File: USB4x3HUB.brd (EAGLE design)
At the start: 70 x 70 mm, 93 parts, among them IC1 IC_USB_TUSB2036, IC10 IC_TTL_SINGLE_74_139_FLAT, IC2 IC_USB_FSUSB74, IC3 IC_POWER_TPS2041C, IC4 IC_POWER_TPS2041C, IC5 IC_POWER_TPS2041C, IC6 LDO4_3.3_SOT223, IC7 LDO4_5.0_SOT223, IC8 LDO4_5.0_SOT223, IC9 LDO4_5.0_SOT223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

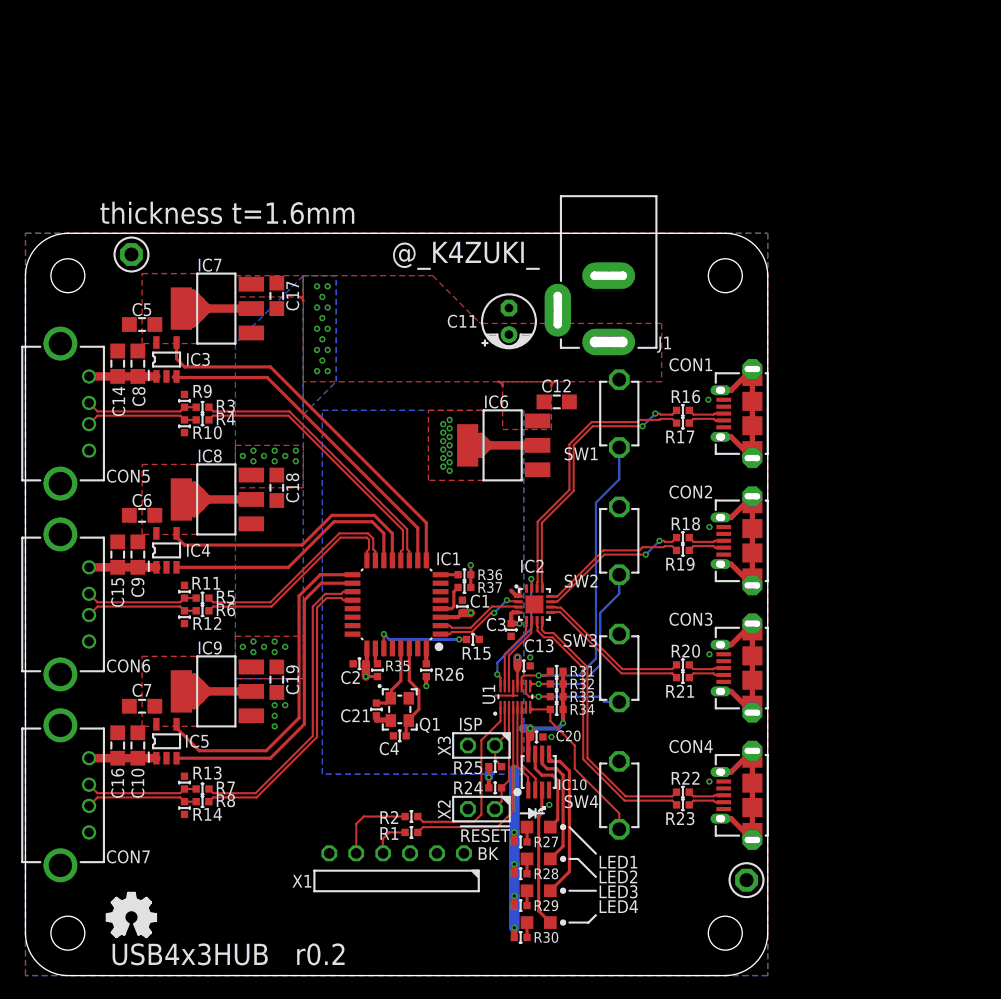
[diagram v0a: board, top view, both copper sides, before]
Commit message: [ r0.3 ] move IC1 and surroundings; replace U1 to use TSSOP(JDH16); ICON_REVISION
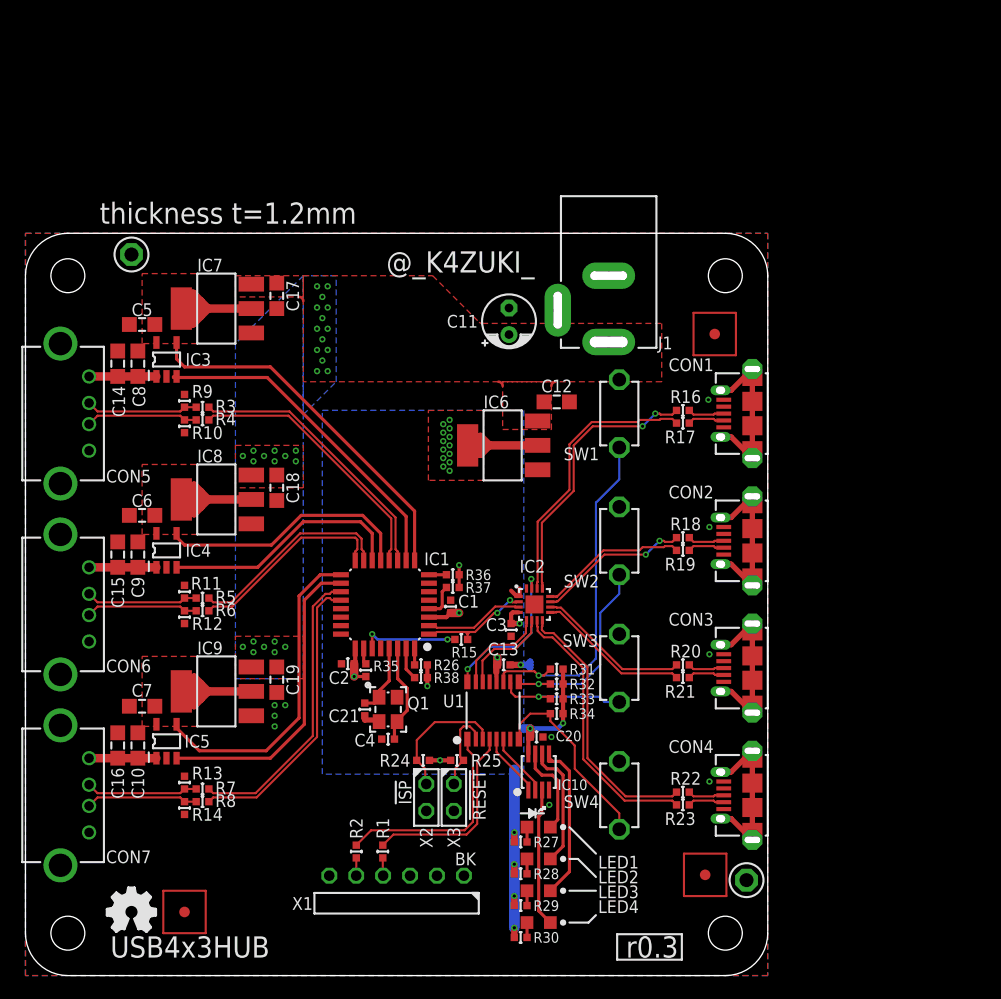
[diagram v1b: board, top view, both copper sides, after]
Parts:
- removed U$1: ICON_OSHW, mylib:ICON_OSHW
- added ICON1: OSHW, mylib:ICON_OSHW
- added ICON2: r0.3, mylib:ICON_REVISION
- added R38: (no value), mylib:C0402
- added TP100, TP101, TP102: (no value), mylib:FIDUCIAL
- IC1: value IC_USB_TUSB2036 -> (none)
- IC2: value IC_USB_FSUSB74 -> (none)
- IC3, IC4, IC5: value IC_POWER_TPS2041C -> (none)
- IC6: value LDO4_3.3_SOT223 -> 3.3V
- IC7, IC8, IC9: value LDO4_5.0_SOT223 -> 5V
- LED1: value (none) -> RD
- LED2: value (none) -> BL
- LED3: value (none) -> GR
- LED4: value (none) -> YL
- Q1: value (none) -> 48M/3225; device mylib:CLOCK_2520 -> mylib:CLOCK_3225
- SW1: value TACTSW2_RD_P807X -> RD
- SW2: value TACTSW2_BL_P807X -> BL
- SW3: value TACTSW2_GR_P807X -> GR
- SW4: value TACTSW2_YL_P807X -> YL
- U1: value IC_LPC81X_16 -> LPC812M101JDH16; device mylib:XSON16_0.4P3.2X2.5 -> mylib:SOT65P510X450X110-16N
- moved R24 7.28 mm to (37.5, 20.3), turned to 0 degrees
- moved R2 6.16 mm to (31.2, 11.7), turned to 90 degrees
- moved X3 5.55 mm to (40.4, 16.8), turned to 90 degrees
- moved X2 5.32 mm to (37.8, 16.8), turned to 90 degrees
- moved R25 3.65 mm to (40.7, 20.3)
- moved R1 3.24 mm to (33.7, 11.7), turned to 90 degrees
- moved U1 2.47 mm to (44.1, 25.0), turned to 0 degrees
- moved X1 2.10 mm to (35.0, 7.90)
- moved C13 1.90 mm to (45.1, 29.3)
- moved C4 1.14 mm to (34.2, 22.3)
- moved C1 1.10 mm to (40.1, 34.8)
- moved C2 1.10 mm to (30.4, 29.4)
- moved C21 1.10 mm to (32.0, 25.1)
- moved IC1 1.10 mm to (33.9, 35.0)
- moved R15 1.10 mm to (41.1, 31.7)
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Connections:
- new net N$63: IC1.31, R38.2
- net 3.3V: now also R38.1
- net GND: no longer IC1.31
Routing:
- net <-RX: track 7.67 -> 1.68 mm
- net N$63: track 0.00 -> 3.08 mm
- net TGT_TX: track 17.3 -> 19.9 mm
- net !RESET!: track 10.2 -> 12.7 mm
- net LSEL2: track 8.35 -> 6.04 mm
- net !OE!: track 12.5 -> 14.7 mm
- net LSEL1: track 8.22 -> 6.04 mm
- net ->TX: track 3.79 -> 1.69 mm
- net SEL1: track 7.05 -> 9.01 mm
- net SW1: track 30.6 -> 32.6 mm
- net ISP: track 6.24 -> 8.19 mm
- net SW3: track 10.9 -> 12.8 mm
- net SEL0: track 7.09 -> 8.91 mm
- net SW4: track 16.7 -> 18.4 mm
- net TGT_RX: track 19.6 -> 18.2 mm
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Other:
- board text added: "!ISP!"
- board text added: "thickness t=1.2mm"
- board text removed: "ISP"
- board text removed: "r0.2"
- board text removed: "thickness t=1.6mm"

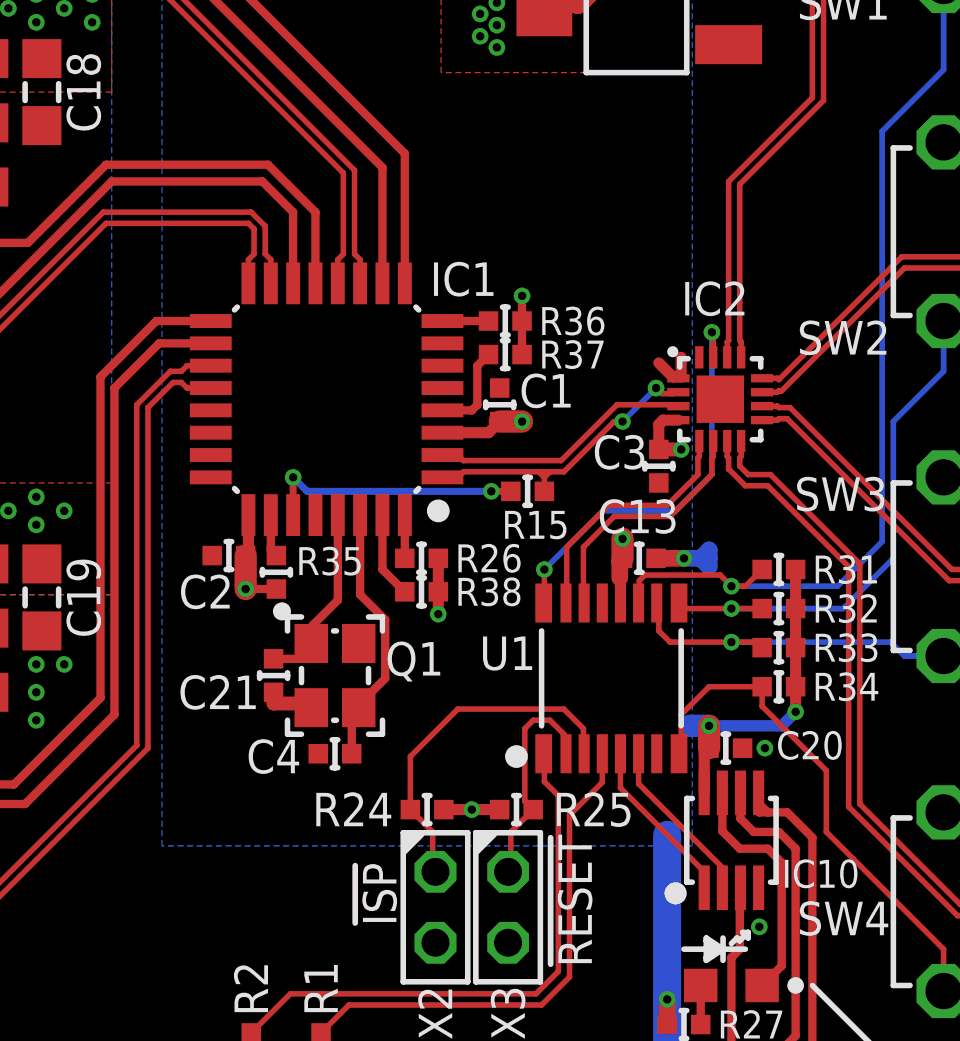
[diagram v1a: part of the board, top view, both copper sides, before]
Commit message: [ r0.3 ] update BOM; fix HUB BUS line
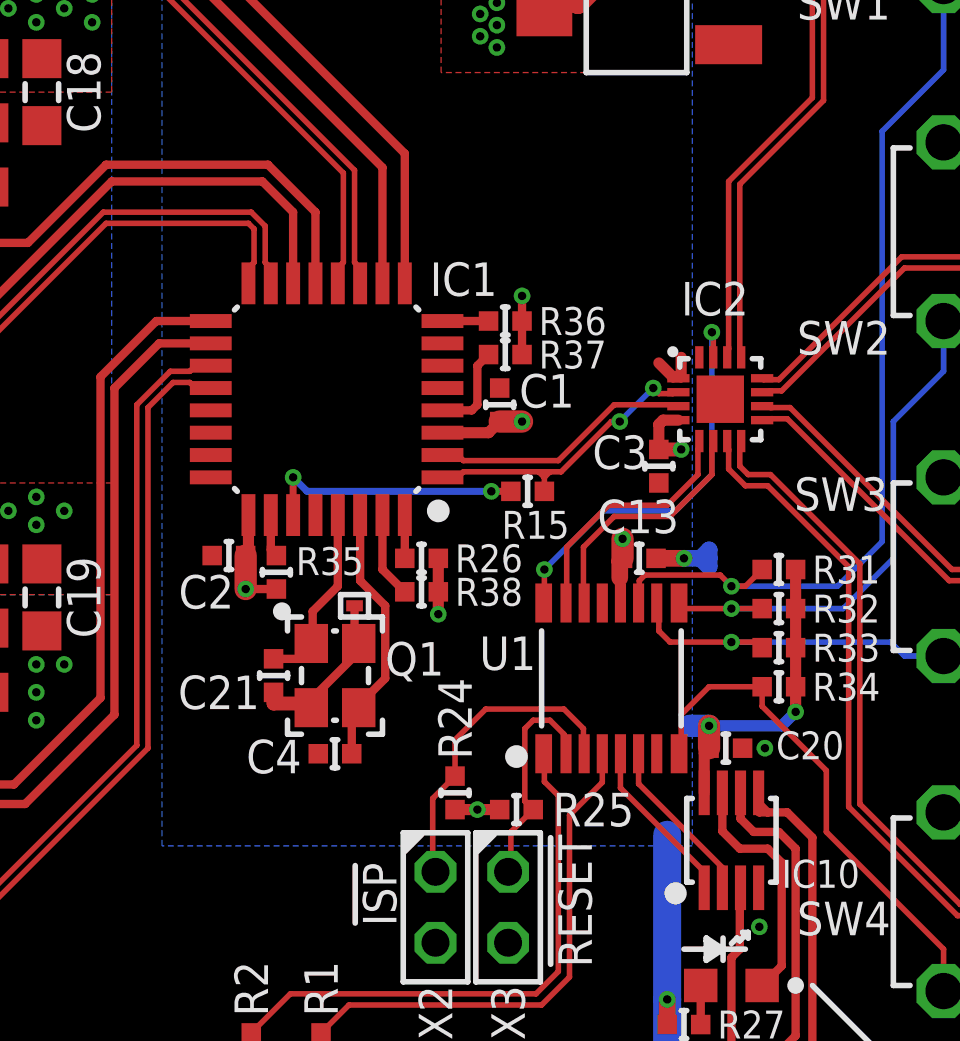
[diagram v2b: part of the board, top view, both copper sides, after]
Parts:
- added TP3: (no value), mylib:TP06RECT
- added U$1: e64d5c4, git-revision:GIT-REVISION
- R15: value (none) -> 1.5k/1005
- moved R24 1.17 mm to (38.5, 20.9), turned to 270 degrees
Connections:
- net GND: now also TP3.TP
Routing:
- net GND: track 6.91 -> 11.3 mm
- net !RESET!: track 12.7 -> 11.4 mm

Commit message: [ r0.3 ] library update
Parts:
- GIT1: value e64d5c4 -> 9ed6508
- IC10: value IC_TTL_SINGLE_74_139_FLAT -> SN74LVC1G139DCUR
- ICON2: device mylib:ICON_REVISION -> mylib:ICON_REVISION2.0
- TP1, TP2: value TPPAD1-13 -> (none); device testpad_local:P1-13 -> mylib:TP_4020
- turned TP1 to 90 degrees
- renumbered U$1 to GIT1

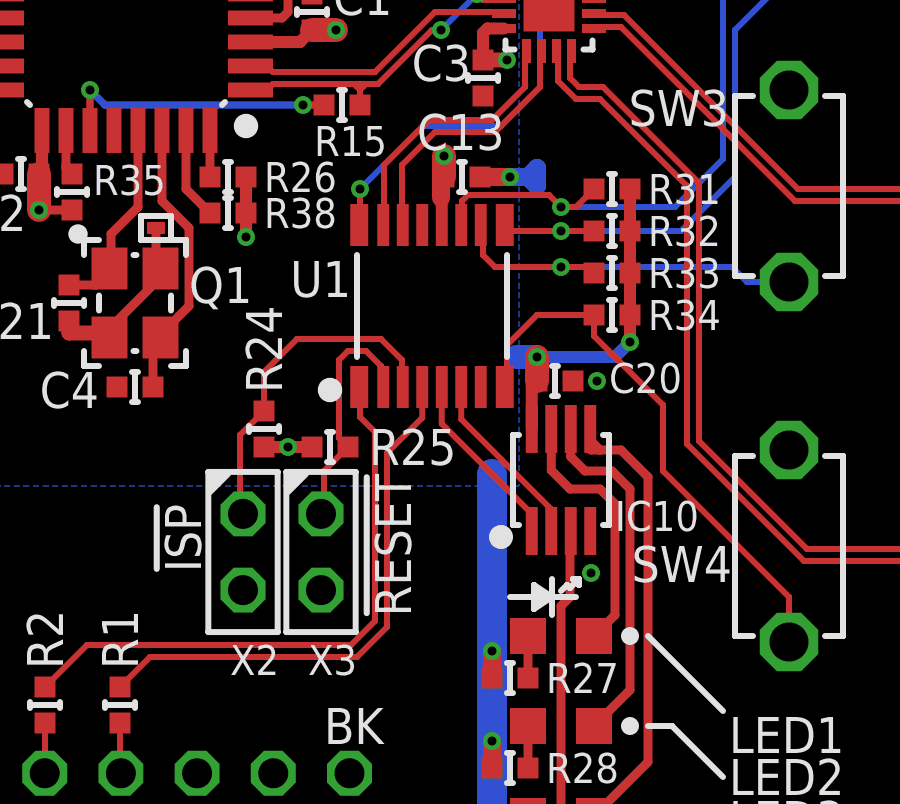
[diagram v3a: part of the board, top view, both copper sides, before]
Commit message: [ r0.3 ] change NAME labels alignment to center; fix UART pins P0_0 and P0_4 must be used for UART as they are used by ISP
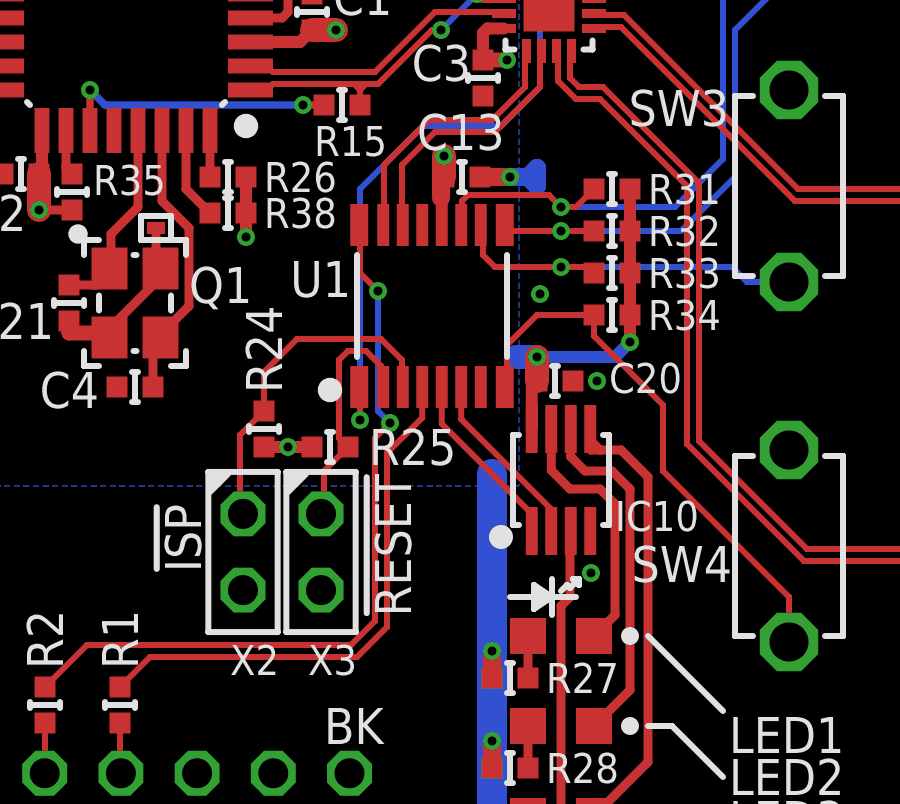
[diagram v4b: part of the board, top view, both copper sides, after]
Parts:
- GIT1: value 9ed6508 -> 215f3cd
- IC1: value (none) -> TUSB2036
- IC2: value (none) -> FSUSB74MPX
- J1: value CON_DCJACK_C1604 -> (none)
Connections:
- net N$30 renamed VCC
- net !OE!: now also U1.1; no longer U1.16
- net TGT_TX: now also U1.16; no longer U1.1
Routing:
- net !OE!: track 14.7 -> 22.2 mm
- net TGT_TX: track 19.9 -> 25.8 mm, vias 0 -> 2
- net GND: vias 11 -> 12
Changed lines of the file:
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@@
 </autorouter>
 <elements>
-<element name="IC1" library="mylib" package="QFP32_0.8P7.2X7.2" value="" x="33.9" y="35" smashed="yes" rot="R180">
+<element name="IC1" library="mylib" package="QFP32_0.8P7.2X7.2" value="TUSB2036" x="33.9" y="35" smashed="yes" rot="R180">
 <attribute name="NAME" x="37.6" y="38.7" size="1.2" layer="25" font="vector" ratio="17"/>
 <attribute name="VALUE" x="36.7" y="36.3" size="1" layer="27" font="vector" ratio="20" rot="R180"/>
 <attribute name="DIGIKEY" value="296-27129-1-ND" x="33.9" y="35" size="1.778" layer="27" rot="R180" display="off"/>
 </element>
-<element name="IC2" library="mylib" package="QFN16_0.5P3.0X3.0" value="" x="48" y="35" smashed="yes">
+<element name="IC2" library="mylib" package="QFN16_0.5P3.0X3.0" value="FSUSB74MPX" x="48" y="35" smashed="yes">
 <attribute name="NAME" x="46.6" y="38" size="1.2" layer="25" ratio="17"/>
 <attribute name="DIGIKEY" value="FSUSB74MPXCT-ND" x="48" y="35" size="1.778" layer="27" display="off"/>
@@
 <attribute name="AKIZUKI" value="C-07674" x="6" y="17" size="1.778" layer="27" rot="R270" display="off"/>
 </element>
-<element name="J1" library="mylib" package="CON_DCJACK_C-1604" value="CON_DCJACK_C1604" x="55" y="73.5" smashed="yes" rot="R270">
+<element name="J1" library="mylib" package="CON_DCJACK_C-1604" value="" x="55" y="73.5" smashed="yes" rot="R270">
 <attribute name="VALUE" x="48.65" y="74.19" size="1.27" layer="27" font="vector" rot="R270"/>
 <attribute name="NAME" x="59.64" y="59.06" size="1.2" layer="25" font="vector" ratio="17"/>
@@
 <attribute name="VALUE" x="35.281" y="27.346" size="0.0254" layer="27" rot="R90"/>
 </element>
-<element name="GIT1" library="git-revision" package="GIT-REVISION" value="9ed6508" x="0" y="0"/>
+<element name="GIT1" library="git-revision" package="GIT-REVISION" value="215f3cd" x="0" y="0"/>
 <element name="TP1" library="mylib" package="TP_4020" value="" x="68" y="9" rot="R90">
 <attribute name="DIGIKEY" value="36-5019CT-ND" x="68" y="9" size="1.778" layer="27" rot="R90" display="off"/>
@@
 <wire x1="34.9" y1="27.6" x2="34.9" y2="26.4" width="0.3" layer="1"/>
 <wire x1="34.9" y1="26.4" x2="35.05" y2="26.25" width="0.3" layer="1"/>
+<contactref element="TP1" pad="TP"/>
+<contactref element="TP1" pad="TP"/>
+<contactref element="TP2" pad="TP"/>
+<contactref element="TP2" pad="TP"/>
 <contactref element="CON1" pad="5"/>
 <contactref element="CON2" pad="5"/>
@@
 <contactref element="CON6" pad="4"/>
 <contactref element="CON7" pad="4"/>
-<contactref element="TP1" pad="TP"/>
-<contactref element="TP1" pad="TP"/>
-<contactref element="TP2" pad="TP"/>
-<contactref element="TP2" pad="TP"/>
+<via x="47.7" y="25.4" extent="1-16" drill="0.3"/>
 </signal>
 <signal name="AVSS">
@@
 <contactref element="CON3" pad="1"/>
 </signal>
-<signal name="N$30">
-<contactref element="CON4" pad="1"/>
-</signal>
 <signal name="N$31">
 <contactref element="CON1" pad="SHD$3"/>
@@
 <signal name="!OE!">
 <contactref element="IC2" pad="15"/>
-<contactref element="U1" pad="16"/>
 <via x="47.7" y="37.4" extent="1-16" drill="0.3"/>
 <wire x1="47.75" y1="36.5" x2="47.75" y2="37.35" width="0.2" layer="1"/>
@@
 <wire x1="46.4" y1="31" x2="47.7" y2="32.3" width="0.2" layer="16"/>
 <wire x1="47.7" y1="32.3" x2="47.7" y2="37.4" width="0.2" layer="16"/>
-<wire x1="41.675" y1="27.7" x2="41.7" y2="27.7" width="0.2" layer="1"/>
-<wire x1="41.7" y1="27.7" x2="41.7" y2="28.9" width="0.2" layer="1"/>
-<via x="41.7" y="28.9" extent="1-16" drill="0.3"/>
 <wire x1="41.7" y1="28.9" x2="43.8" y2="31" width="0.2" layer="16"/>
 <wire x1="43.8" y1="31" x2="46.4" y2="31" width="0.2" layer="16"/>
+<contactref element="U1" pad="1"/>
+<wire x1="41.7" y1="28.9" x2="41.7" y2="21.2" width="0.2" layer="16"/>
+<via x="41.7" y="21.2" extent="1-16" drill="0.3"/>
+<wire x1="41.7" y1="21.2" x2="41.7" y2="22.275" width="0.2" layer="1"/>
+<wire x1="41.7" y1="22.275" x2="41.675" y2="22.3" width="0.2" layer="1"/>
 </signal>
 <signal name="SW1">
@@
 <signal name="TGT_TX">
 <contactref element="R2" pad="2"/>
-<contactref element="U1" pad="1"/>
-<wire x1="41.675" y1="22.3" x2="41.7" y2="22.3" width="0.2" layer="1"/>
-<wire x1="41.7" y1="22.3" x2="41.7" y2="21.3" width="0.2" layer="1"/>
-<wire x1="41.7" y1="21.3" x2="42.2" y2="20.8" width="0.2" layer="1"/>
-<wire x1="42.2" y1="20.8" x2="42.2" y2="14.5" width="0.2" layer="1"/>
+<wire x1="42.7" y1="21.1" x2="42.2" y2="20.6" width="0.2" layer="1"/>
+<wire x1="42.2" y1="20.6" x2="42.2" y2="14.5" width="0.2" layer="1"/>
 <wire x1="42.2" y1="14.5" x2="41.4" y2="13.7" width="0.2" layer="1"/>
 <wire x1="41.4" y1="13.7" x2="32.6" y2="13.7" width="0.2" layer="1"/>
 <wire x1="32.6" y1="13.7" x2="31.2" y2="12.3" width="0.2" layer="1"/>
+<contactref element="U1" pad="16"/>
+<wire x1="41.675" y1="27.7" x2="41.7" y2="27.7" width="0.2" layer="1"/>
+<wire x1="41.7" y1="27.7" x2="41.7" y2="26.1" width="0.2" layer="1"/>
+<via x="42.7" y="21.1" extent="1-16" drill="0.3"/>
+<via x="42.3" y="25.5" extent="1-16" drill="0.3"/>
+<wire x1="42.3" y1="25.5" x2="41.7" y2="26.1" width="0.2" layer="1"/>
+<wire x1="42.3" y1="25.5" x2="42.3" y2="21.5" width="0.2" layer="16"/>
+<wire x1="42.3" y1="21.5" x2="42.7" y2="21.1" width="0.2" layer="16"/>
 </signal>
 <signal name="-&gt;TX">
@@
 <wire x1="35.9" y1="28.9" x2="36.7" y2="28.1" width="0.3" layer="1"/>
 </signal>
+<signal name="VCC">
+<contactref element="CON4" pad="1"/>
+</signal>
 </signals>

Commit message: Revision 0.3
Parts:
- moved TP102 51.2 mm to (20.0, 85.0)
- moved C17 14.1 mm to (33.7, 74.1)
- moved C18 14.1 mm to (33.7, 56.0)
- moved C19 14.1 mm to (33.7, 37.9)
- moved C5 14.1 mm to (21.0, 71.4)
- moved IC7 14.1 mm to (28.0, 72.9)
- moved R15 14.1 mm to (51.1, 41.7)
- moved R2 14.1 mm to (41.2, 21.7)
- moved R34 14.1 mm to (60.1, 34.7)
- moved C1 14.1 mm to (50.1, 44.8)
- moved C10 14.1 mm to (20.6, 31.7)
- moved C11 14.1 mm to (55.6, 71.7)
- moved C14 14.1 mm to (18.7, 67.7)
- moved C15 14.1 mm to (18.7, 49.7)
- moved C16 14.1 mm to (18.7, 31.7)
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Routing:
- net N$16: track 31.9 -> 31.3 mm
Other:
- board size 70 x 70 mm -> 90 x 90 mm
- board text added: "V-CUT"
